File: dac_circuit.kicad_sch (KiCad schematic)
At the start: 53 parts, among them J201 Conn_01x02, J202 Conn_02x03_Odd_Even, J203 Conn_01x02, J204 Conn_01x07, U201 LM324, U202 74HC595, U203 74HC595

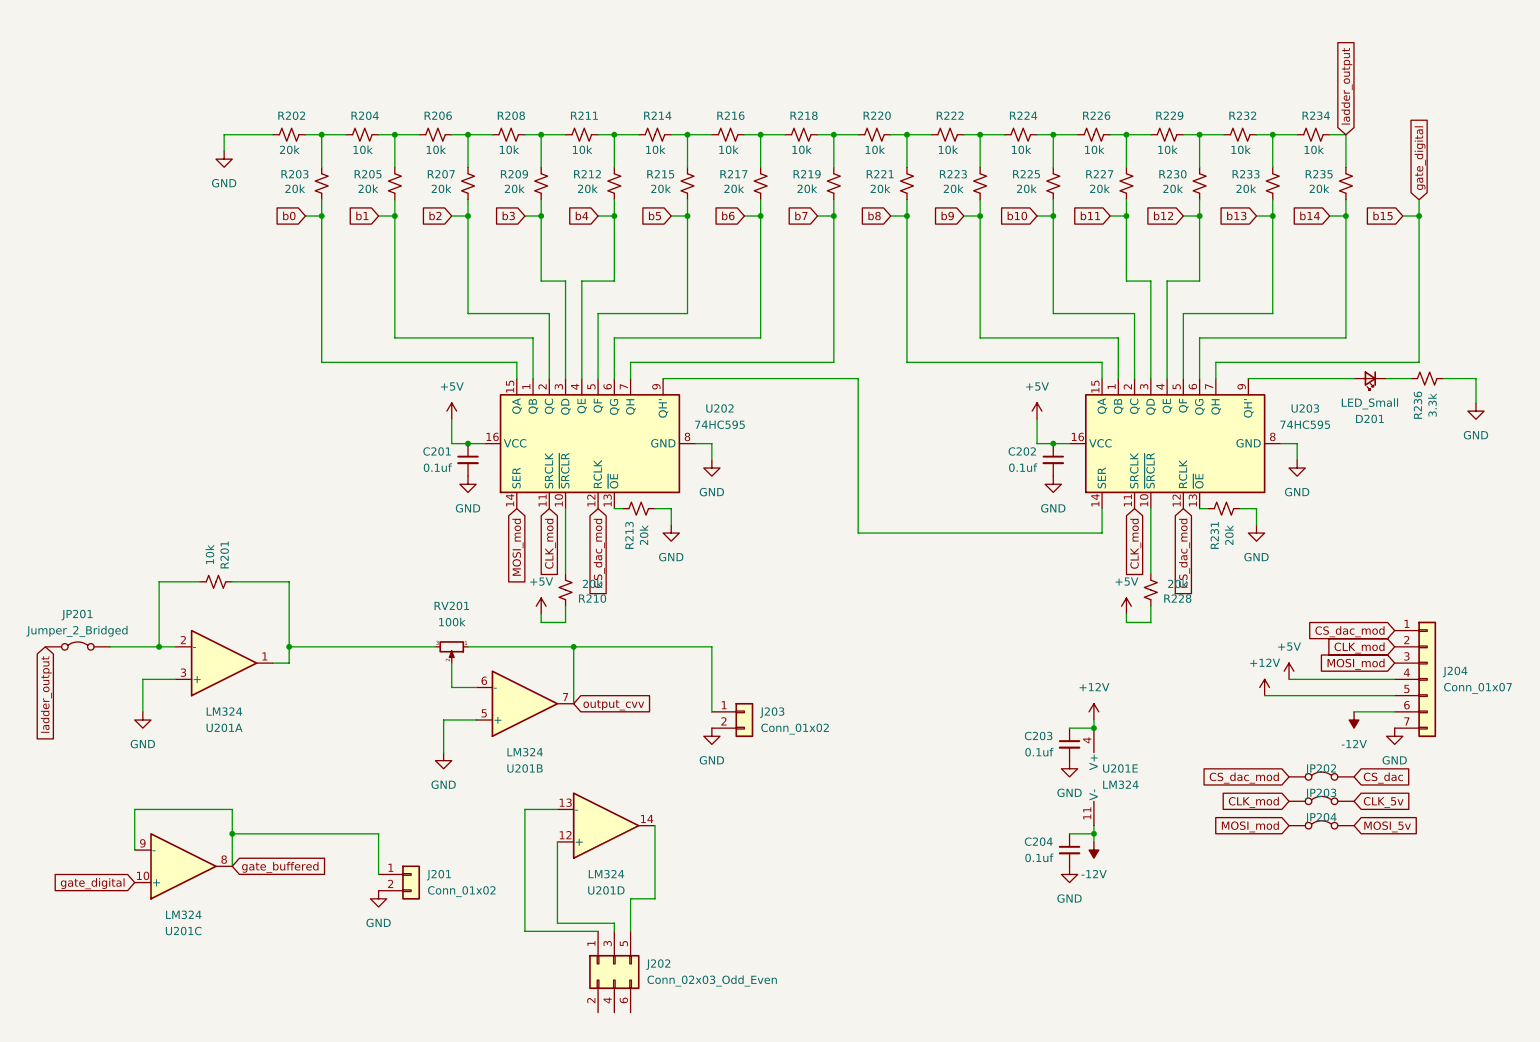
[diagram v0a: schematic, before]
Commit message: schematic done, routed dac ladder
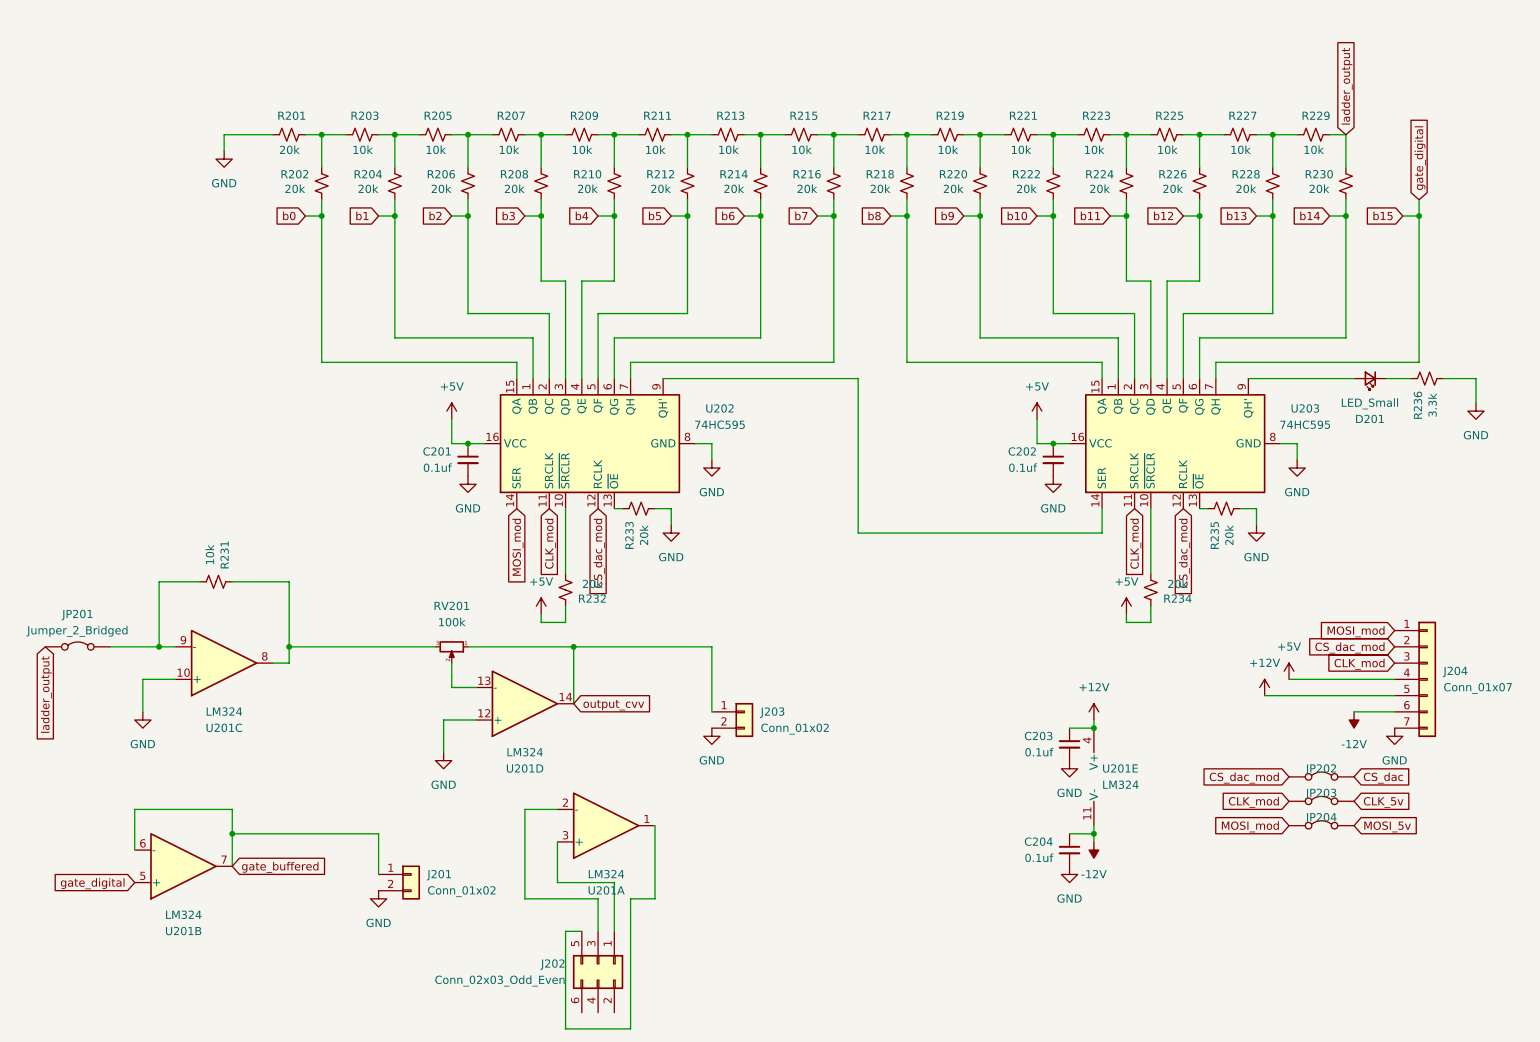
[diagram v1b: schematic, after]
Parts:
- J204: footprint (none) -> Connector_PinSocket_2.54mm:PinSocket_1x07_P2.54mm_Vertical
- JP202: footprint Connector_PinSocket_2.54mm:PinSocket_1x02_P2.54mm_Vertical -> Jumper:SolderJumper-2_P1.3mm_Bridged_RoundedPad1.0x1.5mm
- renumbered R202 to R201, R203 to R202, R204 to R203, R205 to R204, R206 to R205, R207 to R206, R208 to R207, R209 to R208, R211 to R209, R212 to R210, R214 to R211, R215 to R212, R216 to R213, R217 to R214, R218 to R215, R219 to R216, R220 to R217, R221 to R218, R222 to R219, R223 to R220, R224 to R221, R225 to R222, R226 to R223, R227 to R224, R229 to R225, R230 to R226, R232 to R227, R233 to R228, R234 to R229, R235 to R230, R201 to R231, R210 to R232, R213 to R233, R228 to R234, R231 to R235
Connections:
- net CLK_mod: now also J204.3 (Pin_3); no longer J204.2 (Pin_2)
- net CS_dac_mod: now also J204.2 (Pin_2); no longer J204.1 (Pin_1)
- net GND: now also U201.10 (+), U201.12 (+); no longer U201.3 (+), U201.5 (+)
- net MOSI_mod: now also J204.1 (Pin_1); no longer J204.3 (Pin_3)
- net b15: now also U201.5 (+); no longer U201.10 (+)
- net gate_buffered: now also U201.6 (-), U201.7; no longer U201.8, U201.9 (-)
- net output_cvv: now also U201.14; no longer U201.7
- net at R231.2, RV201.3: now also U201.8; no longer U201.1
- net at JP201.2 (B), R231.1: now also U201.9 (-); no longer U201.2 (-)
- net at RV201.2: now also U201.13 (-); no longer U201.6 (-)
- net at J202.1 (Pin_1): now also U201.3 (+); no longer U201.13 (-)
- net at J202.3 (Pin_3): now also U201.2 (-); no longer U201.12 (+)
- net at J202.5 (Pin_5): now also U201.1; no longer U201.14
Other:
- moved on the sheet: J202, U201A, U201B, U201C, U201D

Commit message: added lcsc part numbers and fabrication files
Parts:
- C201, C202, C203, C204: LCSC PN (none) -> C49678
- D201: value LED_Small -> LED; LCSC PN (none) -> C2297
- R201, R202, R204, R206, R208, R210, R212, R214, R216, R218, R220, R222, R224, R226, R228, R230, R232, R233, R234, R235: LCSC PN (none) -> C4328
- R203, R205, R207, R209, R211, R213, R215, R217, R219, R221, R223, R225, R227, R229, R231: LCSC PN (none) -> C17414
- R236: value 3.3k -> 2k; LCSC PN (none) -> C17604
- U202, U203: LCSC PN (none) -> C5947
